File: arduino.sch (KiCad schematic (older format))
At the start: 27 parts, among them P1 CONN_25X2, P10 CONN_3X2, P2 Arduino-Left, P3 Arduino-Bottom, P4 Arduino-FTDI, P5 Arduino_Right, P6 Arduino-Middle, P7 CONN_14, P8 CONN_8, P9 CONN_3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

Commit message: Replace Arduino Pro Mini Clone with an ATMega32A instead
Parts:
- removed P2: Arduino-Left, Socket_Strips:Socket_Strip_Straight_1x12, symbol CONN_12
- removed P3: Arduino-Bottom, Socket_Strips:Socket_Strip_Straight_1x03, symbol CONN_3
- removed P4: Arduino-FTDI, Socket_Strips:Socket_Strip_Straight_1x06, symbol CONN_6
- removed P5: Arduino_Right, Socket_Strips:Socket_Strip_Straight_1x12, symbol CONN_12
- removed P6: Arduino-Middle, Socket_Strips:Socket_Strip_Straight_1x02, symbol CONN_2
- removed P7: CONN_14, Socket_Strips:Socket_Strip_Straight_1x14, symbol CONN_14
- added C8: C, Capacitors_ThroughHole:Capacitor3MMDiscRM2.5, symbol C
- added IC1: ATMEGA32A-P, Sockets_DIP:DIP-40__600_ELL, symbol ATMEGA32A-P
- added P1: PORT_D, Socket_Strips:Socket_Strip_Straight_1x08, symbol CONN_8
- added P2: PORT_C, Socket_Strips:Socket_Strip_Straight_1x08, symbol CONN_8
- added P3: PORT_B, Socket_Strips:Socket_Strip_Straight_1x08, symbol CONN_8
- P4: renamed from P8; value CONN_8 -> PORT_A
- P5: renamed from P10; value CONN_3X2 -> ISP; footprint Pin_Headers:Pin_Header_Straight_2x03 -> Socket_Strips:Socket_Strip_Straight_2x03
- P6: renamed from P9; value CONN_3 -> PWR
- P7: renamed from P1; value CONN_25X2 -> BUS
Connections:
- net labels added: CLRWT, DT0, DT1, DT14, DT15, DT16, DT17, DT18, DT19, DT20, DT21, DT22, DT23
- net labels removed: DT8, DT9, DTR, RAW
- wire segments 243 -> 259
- no-connect marks 32 -> 31
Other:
- note removed: "Arduino Pro Mini Clone"
- moved on the sheet: P4, P5, P6, U5

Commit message: Silkscreen texts and a jumper to select system clock or feed a separate one for the AVR
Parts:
- added JP1: JUMPER, Socket_Strips:Socket_Strip_Straight_1x02, symbol JUMPER
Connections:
- net labels added: XTAL
- wire segments 259 -> 261
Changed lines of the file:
@@
 	2000 2200 2300 2200
-Wire Wire Line
-	2000 2600 2500 2600
 Wire Wire Line
 	2000 2700 2300 2700
@@
 NoConn ~ 2600 2200
 NoConn ~ 2600 1400
-Wire Wire Line
-	2500 2600 2500 1800
-Wire Wire Line
-	2500 1800 2600 1800
 Wire Wire Line
 	2600 1000 2400 1000
@@
 Text Label 5800 2350 1    60   ~ 0
 GND
+Wire Wire Line
+	2000 2600 2300 2600
+Wire Wire Line
+	2600 1800 2550 1800
+Wire Wire Line
+	2550 1800 2550 2100
+Text Label 2550 2050 1    60   ~ 0
+XTAL
+$Comp
+L JUMPER JP1
+U 1 1 53F116F2
+P 5050 6900
+F 0 "JP1" H 5050 7050 60  0000 C CNN
+F 1 "JUMPER" H 5050 6820 40  0000 C CNN
+F 2 "Socket_Strips:Socket_Strip_Straight_1x02" H 5050 6900 60  0001 C CNN
+F 3 "" H 5050 6900 60  0000 C CNN
+	1    5050 6900
+	1    0    0    -1
+$EndComp
+Wire Wire Line
+	4750 6900 4350 6900
+Wire Wire Line
+	5350 6900 5800 6900
+Text Label 4450 6900 0    60   ~ 0
+CLK
+Text Label 5500 6900 0    60   ~ 0
+XTAL
 $EndSCHEMATC

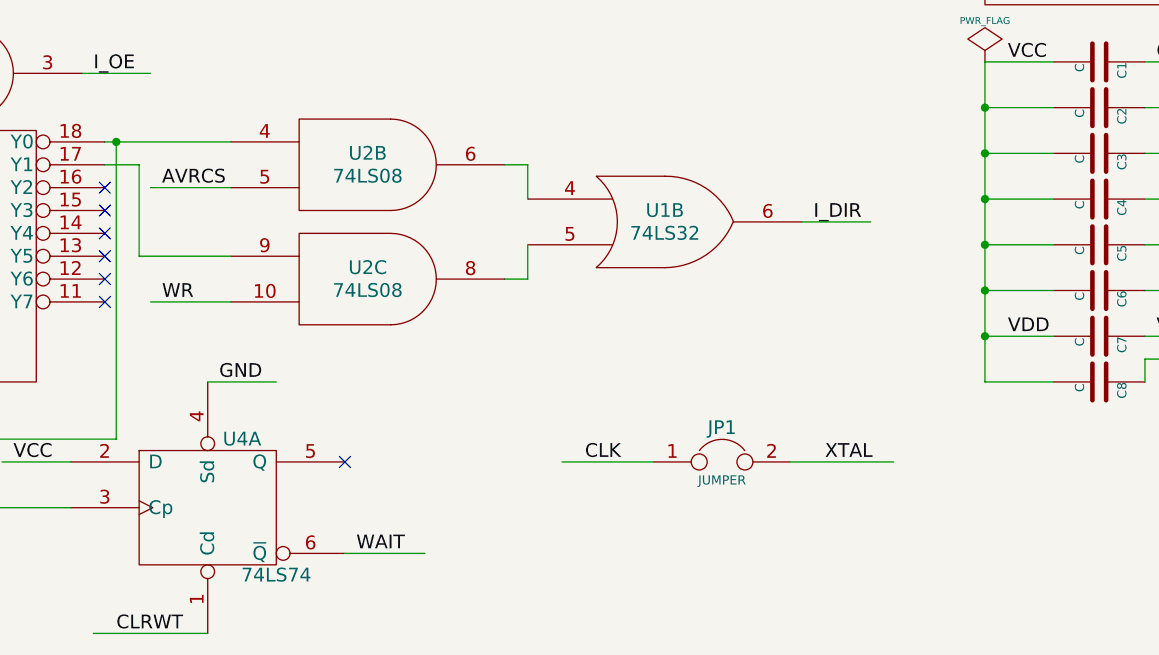
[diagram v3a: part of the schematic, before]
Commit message: Fix a bug and add an FTDI connector
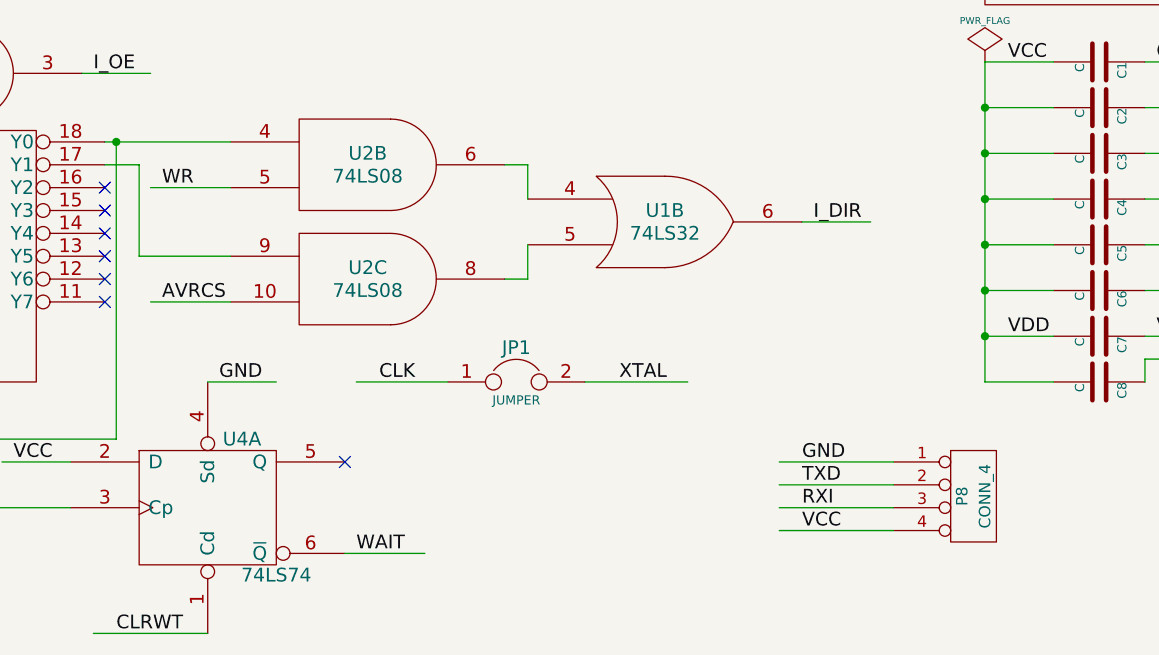
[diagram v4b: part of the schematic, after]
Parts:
- added P8: CONN_4, Socket_Strips:Socket_Strip_Straight_1x04, symbol CONN_4
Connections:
- wire segments 261 -> 265
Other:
- moved on the sheet: JP1
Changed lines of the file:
@@
 Wire Wire Line
 	2900 6200 2550 6200
+Text Label 2600 6200 0    60   ~ 0
+AVRCS
 Text Label 2600 5700 0    60   ~ 0
-AVRCS
-Text Label 2600 6200 0    60   ~ 0
 WR
 Wire Wire Line
@@
 L JUMPER JP1
 U 1 1 53F116F2
-P 5050 6900
-F 0 "JP1" H 5050 7050 60  0000 C CNN
-F 1 "JUMPER" H 5050 6820 40  0000 C CNN
-F 2 "Socket_Strips:Socket_Strip_Straight_1x02" H 5050 6900 60  0001 C CNN
-F 3 "" H 5050 6900 60  0000 C CNN
-	1    5050 6900
-	1    0    0    -1
-$EndComp
-Wire Wire Line
-	4750 6900 4350 6900
-Wire Wire Line
-	5350 6900 5800 6900
-Text Label 4450 6900 0    60   ~ 0
+P 4150 6550
+F 0 "JP1" H 4150 6700 60  0000 C CNN
+F 1 "JUMPER" H 4150 6470 40  0000 C CNN
+F 2 "Socket_Strips:Socket_Strip_Straight_1x02" H 4150 6550 60  0001 C CNN
+F 3 "" H 4150 6550 60  0000 C CNN
+	1    4150 6550
+	1    0    0    -1
+$EndComp
+Wire Wire Line
+	3850 6550 3450 6550
+Wire Wire Line
+	4450 6550 4900 6550
+Text Label 3550 6550 0    60   ~ 0
 CLK
-Text Label 5500 6900 0    60   ~ 0
+Text Label 4600 6550 0    60   ~ 0
 XTAL
+$Comp
+L CONN_4 P8
+U 1 1 54031378
+P 6150 7050
+F 0 "P8" V 6100 7050 50  0000 C CNN
+F 1 "CONN_4" V 6200 7050 50  0000 C CNN
+F 2 "Socket_Strips:Socket_Strip_Straight_1x04" H 6150 7050 60  0001 C CNN
+F 3 "" H 6150 7050 60  0000 C CNN
+	1    6150 7050
+	1    0    0    -1
+$EndComp
+Wire Wire Line
+	5800 6900 5300 6900
+Wire Wire Line
+	5800 7000 5300 7000
+Wire Wire Line
+	5800 7100 5300 7100
+Wire Wire Line
+	5800 7200 5300 7200
+Text Label 5400 7000 0    60   ~ 0
+TXD
+Text Label 5400 7100 0    60   ~ 0
+RXI
+Text Label 5400 6900 0    60   ~ 0
+GND
+Text Label 5400 7200 0    60   ~ 0
+VCC
 $EndSCHEMATC

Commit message: Fix error with ISP port, and move data bus control from PortA to free that one up
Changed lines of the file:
@@
 Text Label 750  5100 0    60   ~ 0
 AVRCS
-Text Label 750  5300 0    60   ~ 0
-AN0
 Wire Wire Line
 	2250 5200 2550 5200
@@
 Wire Wire Line
 	10600 4350 10900 4350
-Text Label 9550 4150 0    60   ~ 0
+Text Label 9550 4350 0    60   ~ 0
 DT6
 Text Label 9550 4250 0    60   ~ 0
@@
 Text Label 10650 4250 0    60   ~ 0
 DT5
-Text Label 9550 4350 0    60   ~ 0
+Text Label 9550 4150 0    60   ~ 0
 RST
+Text Label 10650 4350 0    60   ~ 0
+VCC
 Text Label 10650 4150 0    60   ~ 0
-VCC
-Text Label 10650 4350 0    60   ~ 0
 GND
 $Comp
@@
 Text Label 5400 7200 0    60   ~ 0
 VCC
+Text Label 750  5300 0    60   ~ 0
+DT20
 $EndSCHEMATC

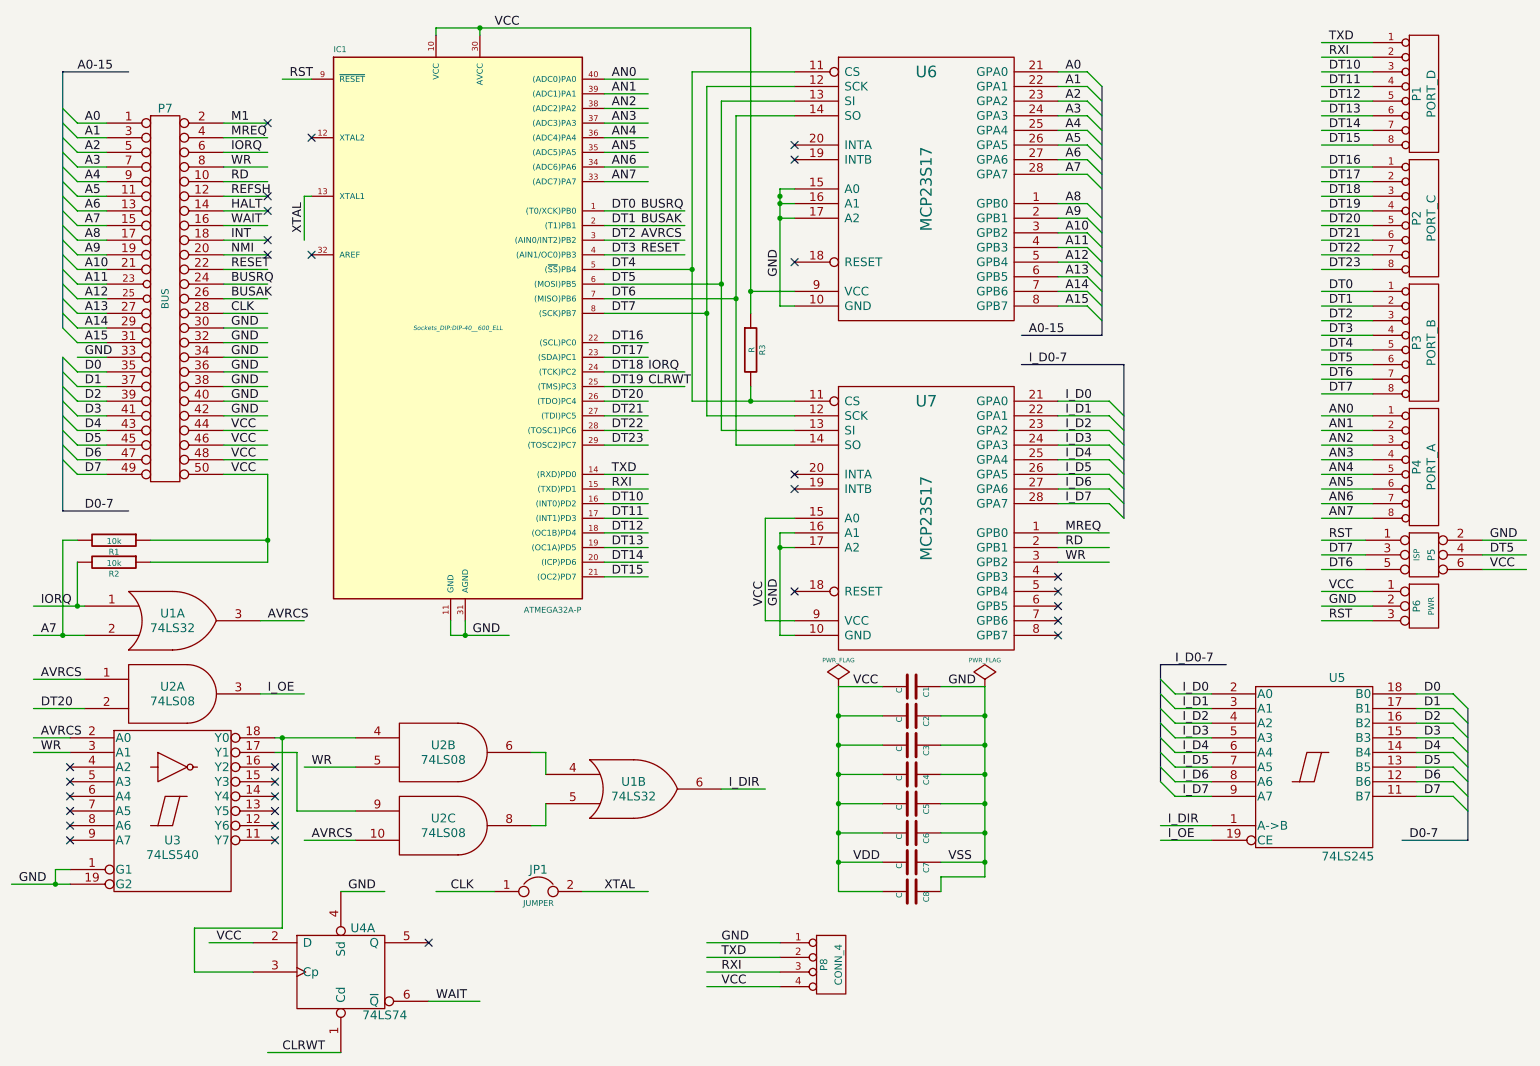
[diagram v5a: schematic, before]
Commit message: Move some pins from AVR to one of the MCP:s to free up PORT A, C and D
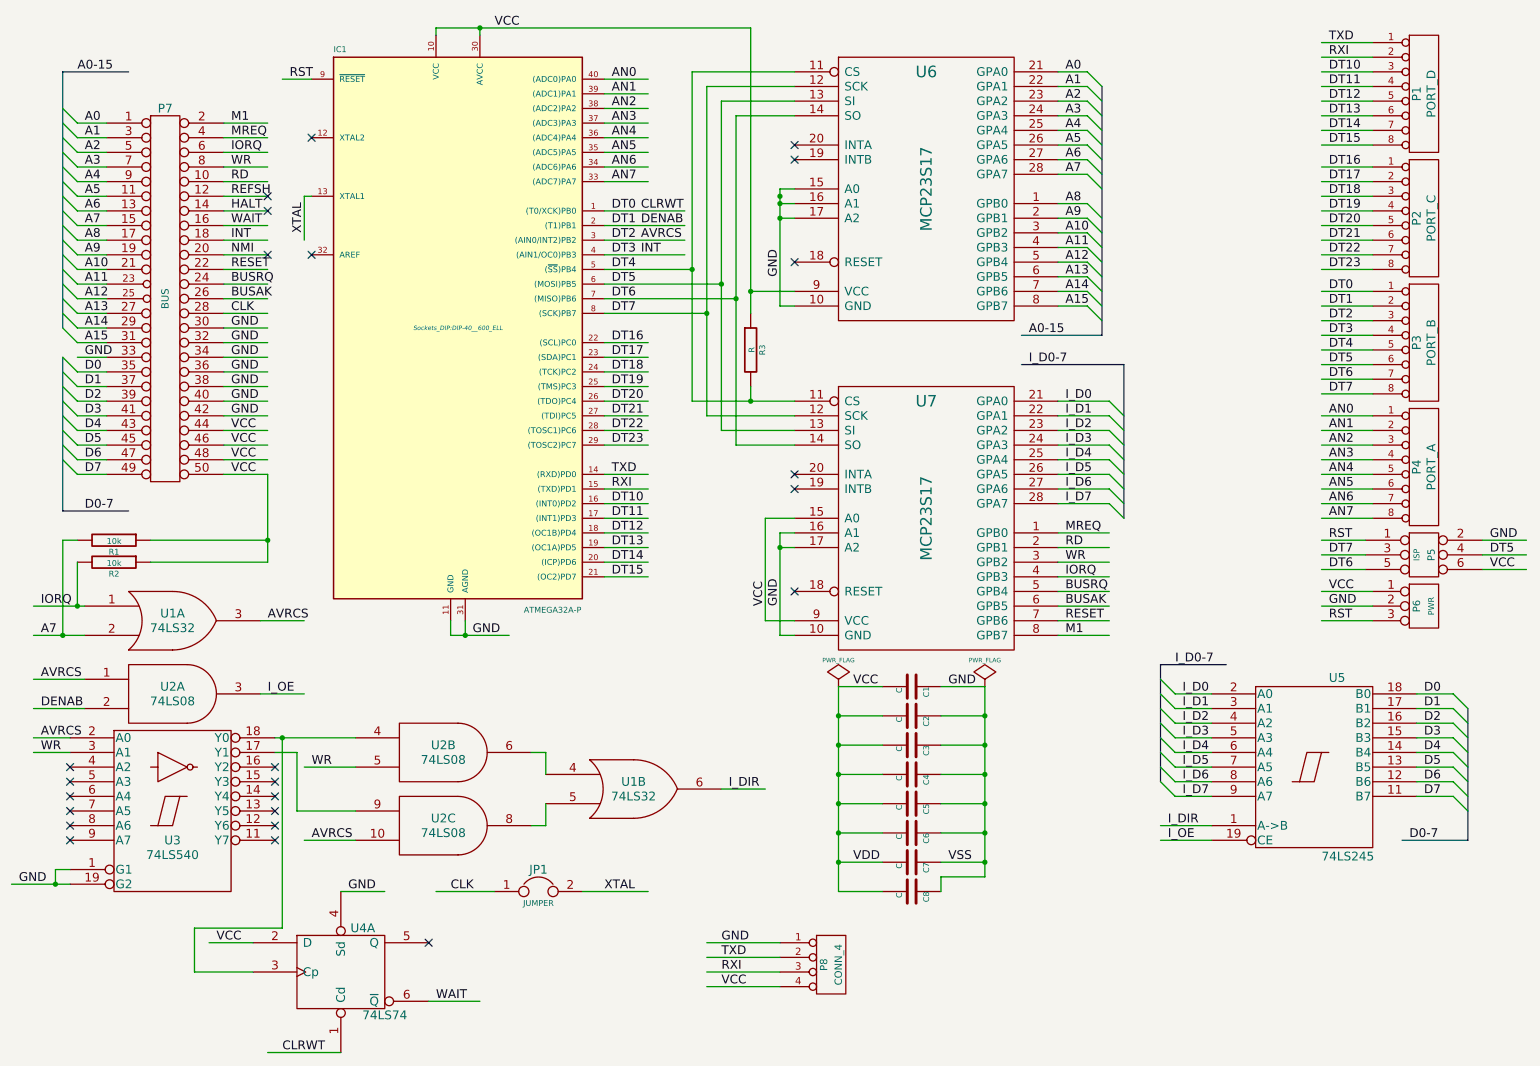
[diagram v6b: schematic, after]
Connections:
- net labels added: DENAB
- wire segments 265 -> 270
- no-connect marks 31 -> 24
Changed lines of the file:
@@
 NoConn ~ 5900 1450
 NoConn ~ 5900 1550
-NoConn ~ 7700 4400
-NoConn ~ 7700 4500
-NoConn ~ 7700 4600
-NoConn ~ 7700 4700
-NoConn ~ 7700 4800
 Wire Wire Line
 	5400 1150 5400 3400
@@
 	7200 6350 6900 6350
 Connection ~ 7200 6150
-NoConn ~ 2300 1300
 NoConn ~ 2300 1900
 $Comp
@@
 NoConn ~ 5900 2250
 NoConn ~ 5900 4500
-NoConn ~ 2300 2100
 NoConn ~ 2300 1800
 NoConn ~ 2300 2200
@@
 Wire Wire Line
 	4600 2900 4900 2900
-Wire Wire Line
-	4600 3000 5150 3000
-Wire Wire Line
-	4600 3100 5150 3100
 Wire Wire Line
 	4600 3200 4900 3200
@@
 Text Label 4850 2100 0    60   ~ 0
 AVRCS
-Text Label 4850 1900 0    60   ~ 0
+Text Label 7750 4500 0    60   ~ 0
 BUSRQ
-Text Label 4850 2000 0    60   ~ 0
+Text Label 7750 4600 0    60   ~ 0
 BUSAK
-Text Label 4850 2200 0    60   ~ 0
+Text Label 7750 4700 0    60   ~ 0
 RESET
 Wire Wire Line
 	4600 1100 4900 1100
-Text Label 4900 3000 0    60   ~ 0
+Text Label 7750 4400 0    60   ~ 0
 IORQ
 $Comp
@@
 Wire Wire Line
 	2000 2500 2300 2500
-Text Label 4900 3100 0    60   ~ 0
+Text Label 4850 1900 0    60   ~ 0
 CLRWT
 Text Label 2400 7650 0    60   ~ 0
@@
 VCC
 Text Label 750  5300 0    60   ~ 0
-DT20
+DENAB
+Wire Wire Line
+	7700 4400 8050 4400
+Wire Wire Line
+	7700 4500 8050 4500
+Wire Wire Line
+	7700 4600 8050 4600
+Wire Wire Line
+	7700 4700 8050 4700
+Wire Wire Line
+	4600 3000 4900 3000
+Wire Wire Line
+	4600 3100 4900 3100
+Text Label 4850 2000 0    60   ~ 0
+DENAB
+Text Label 4850 2200 0    60   ~ 0
+INT
+Text Label 7750 4800 0    60   ~ 0
+M1
+Wire Wire Line
+	7700 4800 8050 4800
 $EndSCHEMATC
